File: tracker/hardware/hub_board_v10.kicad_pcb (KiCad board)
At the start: 2 copper layers, 72 x 80 mm, 28 parts, among them U1 U1, U2 U2, U3 U3, U5 U5, U6 U6, U7 U7

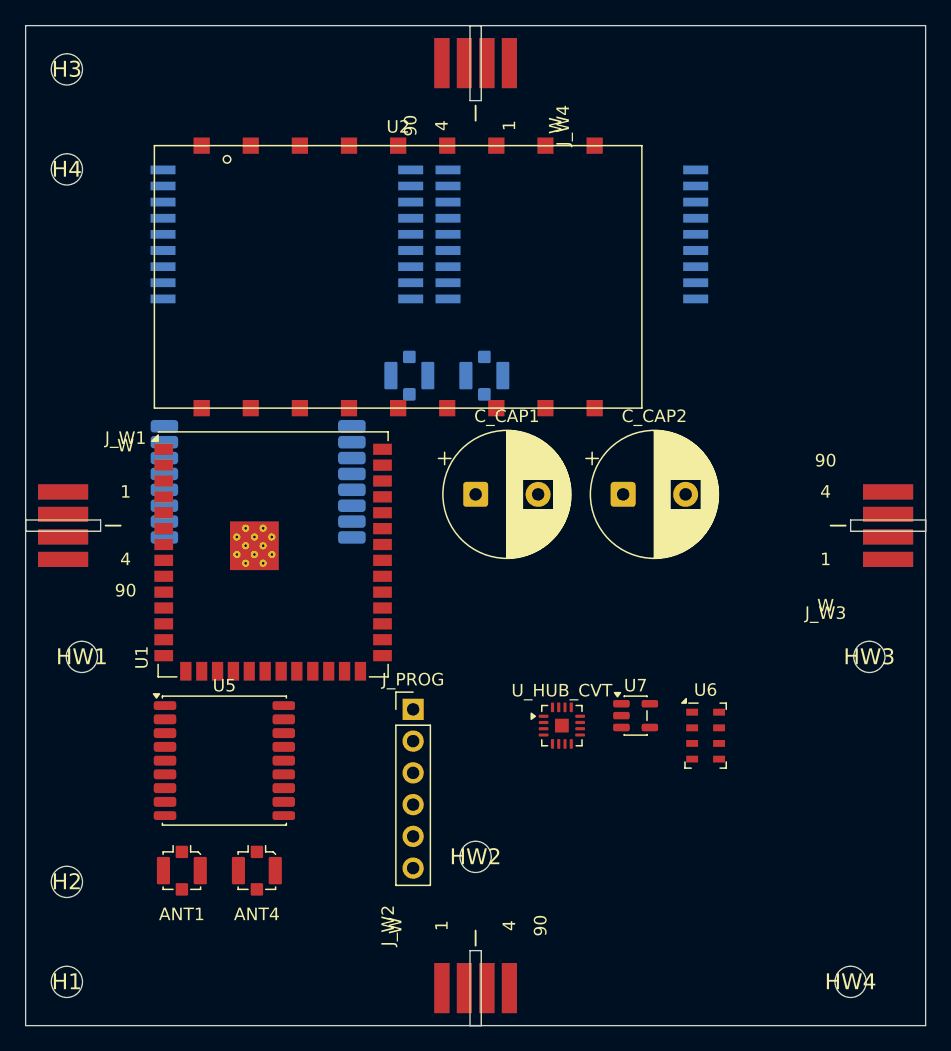
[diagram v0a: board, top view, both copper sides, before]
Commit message: feat(v10): ADR-126 grid A* router with via support -- the ONLY permitted routing method
Operator directive 2026-10-21: "(a) a real grid/A* router with via support -- proper phase 2,
can handle this density. Yes please do this. Please make sure this approach is taken in all
future attempts so that we don't repeat our mistakes. Update agents.md and the tools +
quality gates on the default branch accordingly."

NEW ROUTER -- tracker/hardware/route_v10_astar.py
  grid 0.1mm over the outline; F.Cu + B.Cu; via 0.50/0.25 (measured legal minimum) at a
  25-step cost so vias are used only when they pay; A* with a Manhattan heuristic, bend
  penalty, and obstacle model from the registry (unnamed pads INCLUDED -- they are metal);
  NPTH holes grown by 0.5mm (ADR-125); bodies blocked on their own side; edge keep-out.
  Own-pad exception is a 0.35mm halo that never clears a neighbouring pad's clearance ring.
  Endpoints start/finish on their own pad's layer; the via is inserted automatically.
  The router SELF-VALIDATES the plan in memory (validate_plan) before writing any copper,
  so it cannot emit copper the gates would reject.

MEASURED RESULT (this commit's board):
  routed 11 nets, failed 28 (reported, never forced)
  check_lane_clearance   UNDER-CLEARANCE: 0   (181 TIGHT, i.e. legal but < 0.5mm)
  check_lane_integrity   VIOLATIONS: 0
  check_copper_under_body crossings: 0
  check_hole_clearance   0 violations
  First copper on this board that passes every gate.

BANNED: route_v10_phase1.py (straight/L) is now marked NEGATIVE REFERENCE ONLY in its
header. It produced the U_C.9 short, two dead-end stubs and 21.66mm through the F33 body;
with corrected gates it could place 0 legal nets.

BUGS FIXED IN MY OWN ROUTER while making this work (each measured):
  B10 pad rects from GetPosition()+GetSize() ignored rotation -> U1's rotated pads
      overlapped neighbours. Now GetBoundingBox(). Same fix applied to all checkers.
  B11 endpoint layer forced equal -> dead ends at U1.24/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
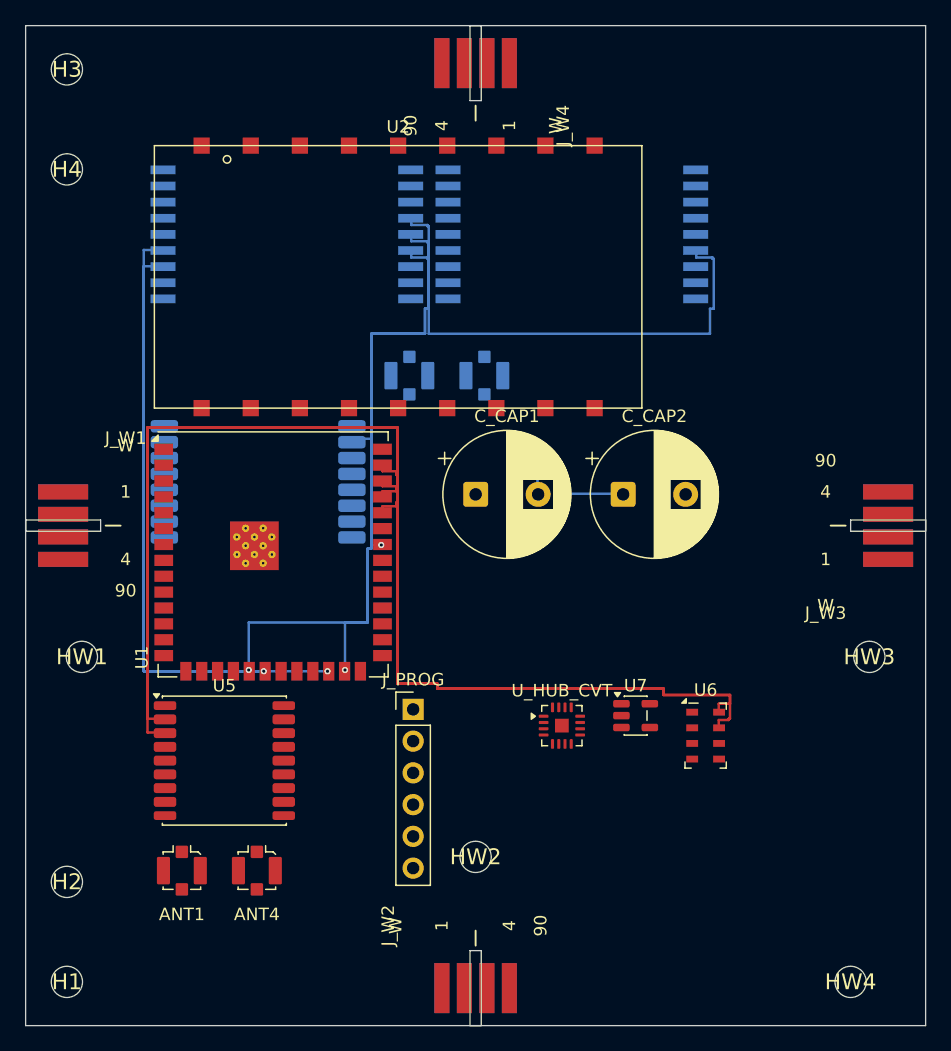
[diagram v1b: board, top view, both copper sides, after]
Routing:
- net /GNSS_TX: track 0.00 -> 52.7 mm
- net /GNSS_RX: track 0.00 -> 52.6 mm
- net /U3_IRQ: track 0.00 -> 52.0 mm, vias 0 -> 1
- net /I2C_SDA: track 0.00 -> 49.7 mm
- net /U3_BUSY: track 0.00 -> 48.7 mm, vias 0 -> 1
- net /I2C_SCL: track 0.00 -> 47.2 mm
- net /U3_CS_N: track 0.00 -> 44.9 mm, vias 0 -> 1
- net /U3_RESET_N: track 0.00 -> 43.0 mm, vias 0 -> 1
- net /VTCXO_VNTC: track 0.00 -> 39.0 mm
- net /E28_DIO3: track 0.00 -> 11.2 mm, vias 0 -> 1
- net /SCAP_MID: track 0.00 -> 9.80 mm

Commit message: feat(v10): lane ISOLATION gate (B15/B16) + router marks its own copper as obstacles
THE OPERATOR'S FIRST FINDING, NOW GATED. The operator asked "many nets look like they are
touching pins they shouldn't" and "do you have geometric tooling for detecting and avoiding
this?". Four gates existed and ALL of them were blind to the class that mattered most:
track vs TRACK. Measured on the router's own output: 152 different-net under-clearances on
B.Cu -- /F33_IRQ crossing /F33_RESET_N, /U3_CS_N, USB and GNSS lines at -0.19mm.

ROOT CAUSE (B14): the A* router routed each net INDEPENDENTLY and never marked its own
placed copper as an obstacle for the next net. Each net was individually clean; together
they shorted each other.

FIXES
  B14  after a net is validated and written, its segments and vias are marked into the
       shared grid, grown by CLEAR + half-track. Later nets must route around them.
  B15  NEW GATE tracker/hardware/check_lane_isolation.py -- different-net copper must keep
       CLEAR: track x track (same layer), track x via, via x via. Exit 0/1, every violation
       named with the measured gap. Proven able to fail: it reported 177 violations on the
       board the old gates called clean.
  B16  via placement now reserves CLEAR + VIA_D/2 + TRACK_W/2, and a routed via marks the
       grid with the same radius. Measured before the fix: vias 0.150mm from other nets'
       tracks (14 violations after B14 alone).

MEASURED RESULT (this commit's board):
  routed 5 nets, failed 32 (reported, never forced), rails deferred to pours
  check_lane_clearance    UNDER-CLEARANCE: 0
  check_lane_integrity    VIOLATIONS: 0
  check_copper_under_body crossings: 0
  check_lane_isolation    ISOLATION VIOLATIONS: 0     <-- the new gate
  check_hole_clearance    0 violations

  The routed count FELL from 16 to 5 because the router is now honest: the 11 nets it used
  to place were shorting each other. Fewer clean nets beats more nets that lie.

BINDING: AGENTS.md item 7 now 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
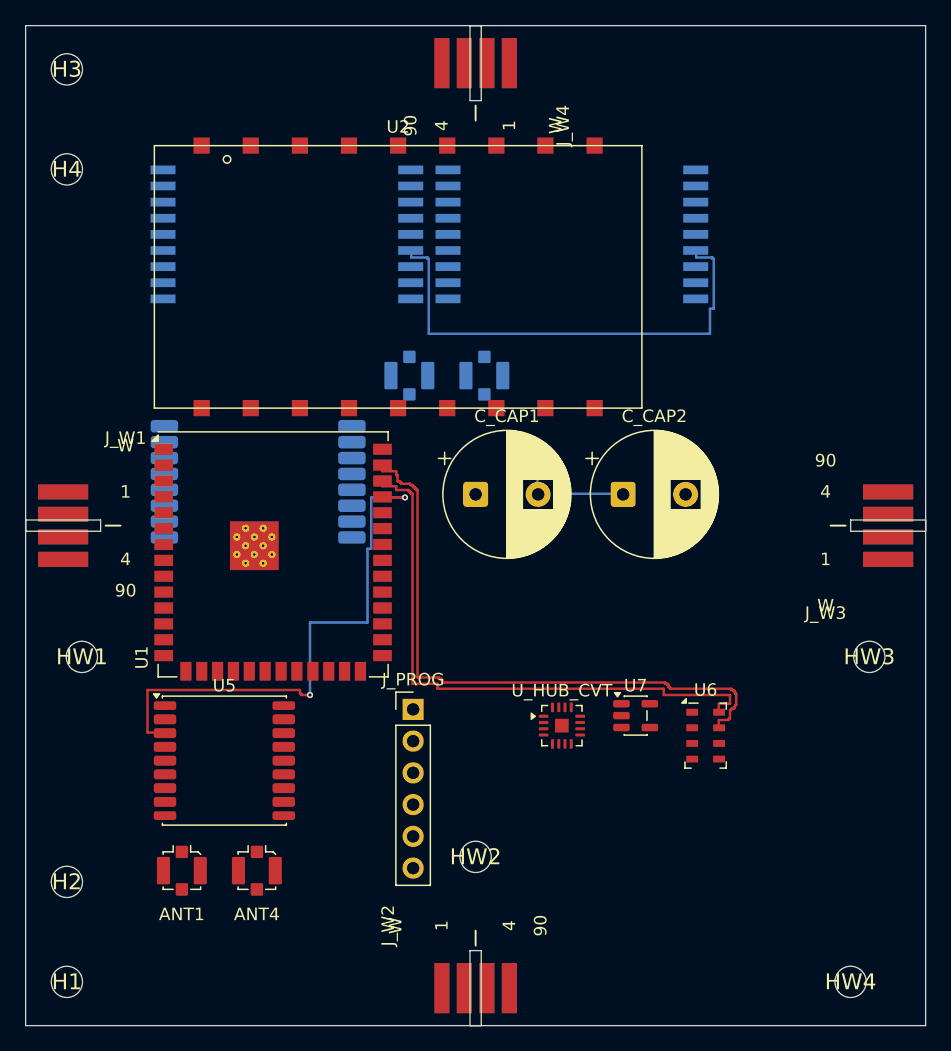
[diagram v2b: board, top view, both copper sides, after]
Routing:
- net /GNSS_TX: track 52.7 -> 0.00 mm
- net /U3_IRQ: track 52.0 -> 0.00 mm, vias 1 -> 0
- net /U3_BUSY: track 48.7 -> 0.00 mm, vias 1 -> 0
- net /U3_CS_N: track 44.9 -> 0.00 mm, vias 1 -> 0
- net /U3_RESET_N: track 43.0 -> 0.00 mm, vias 1 -> 0
- net /E28_DIO3: track 11.2 -> 0.00 mm, vias 1 -> 0
- net /GNSS_RX: track 52.6 -> 43.4 mm, vias 0 -> 2
- net /I2C_SDA: track 49.7 -> 50.7 mm

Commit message: feat(v10): obstacle model corrected to the datasheets (B17/B18) -- 12 nets routed, 5 gates clean
B17 -- THE BLOCKER. The router treated every footprint's COURTYARD box as solid terrain.
U1 (ESP32) and U2 (F33) have 19.5x19.2mm and 39.7x22.3mm courtyards, so the router could
not route anywhere near the two largest parts: measured, EVERY F33 net failed and U1's start
row had 404/722 cells blocked. Reading ADR-118 line 22 and the E28 manual 4.1: ONLY the E28
forbids routing beneath the module. Copper under a castellated/shielded module is normal
practice and KiCad's DRC has no such rule. The obstacle model now blocks a module's box ONLY
for the E28, on BOTH sides (v10 directive 5 makes the E28 keep-out bind both sides).

B18 -- the goal cell. unblock_own() refused to clear a cell inside another pad's clearance
ring, but at U2's 1.27mm pad pitch each neighbour's ring overlaps this pad's CENTRE, so the
endpoint's own middle stayed blocked: measured /F33_CS_N goal cell blocked=1 and every F33
net unroutable. The pad's own INTERIOR is now always reachable; the neighbour-ring guard
applies to the 0.35mm HALO only.

RESULT (this commit's board):
  routed 12 nets: ANT1_433_TX, ANT3_2G4_RX, ANT4_GNSS_L1, F33_BUSY, F33_CS_N, F33_IRQ,
                  F33_RESET_N, GNSS_PPS, SCAP_MID, U3_IRQ, USB_DN, USB_DP
  183 tracks + 16 vias
  lane clearance  UNDER-CLEARANCE: 0
  lane integrity  VIOLATIONS: 0
  under-body      0 (the gate now fires on the E28, the only module with a keep-out rule)
  lane isolation  ISOLATION VIOLATIONS: 0
  hole clearance  0 violations

Also corrected the under-body GATE to match the datasheets (KEEPOUT_REFS = U_E28 only, both
sides). It had been flagging copper beneath U1/U2 -- noise that would have hidden a real E28
violation.
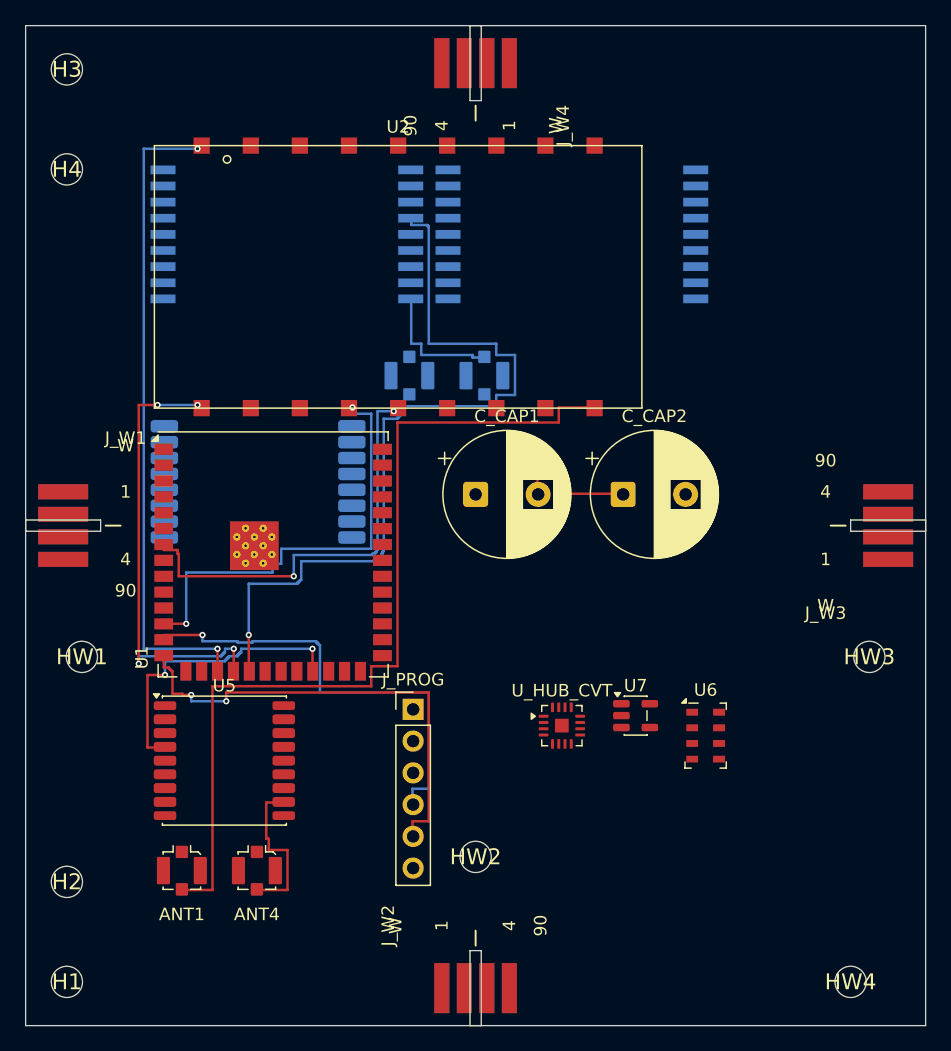
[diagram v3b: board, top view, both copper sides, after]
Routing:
- net /ANT1_433_TX: track 0.00 -> 71.7 mm
- net /U3_IRQ: track 0.00 -> 65.8 mm, vias 0 -> 1
- net /F33_IRQ: track 0.00 -> 52.6 mm, vias 0 -> 2
- net /I2C_SDA: track 50.7 -> 0.00 mm
- net /I2C_SCL: track 47.2 -> 0.00 mm
- net /GNSS_RX: track 43.4 -> 0.00 mm, vias 2 -> 0
- net /VTCXO_VNTC: track 39.0 -> 0.00 mm
- net /USB_DP: track 0.00 -> 38.4 mm, vias 0 -> 2
- net /USB_DN: track 0.00 -> 36.7 mm, vias 0 -> 1
- net /F33_RESET_N: track 0.00 -> 36.5 mm, vias 0 -> 4
- net /F33_BUSY: track 0.00 -> 35.7 mm, vias 0 -> 2
- net /F33_CS_N: track 0.00 -> 34.7 mm, vias 0 -> 2
- net /GNSS_PPS: track 0.00 -> 24.3 mm, vias 0 -> 2
- net /ANT4_GNSS_L1: track 0.00 -> 12.6 mm
- net /ANT3_2G4_RX: track 0.00 -> 10.6 mm

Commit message: fix(v10): move U_E28 off U1 (B22) -- the blocking cross-side collision is GONE
THE FIX. U_E28 was at (18.6, 36.5, 0) on the back -- directly on top of U1 (front):
260.58mm2 shared area and 13 measured pad-to-pad shorts (U1.1/E28.7 ... U1.7/E28.1).

SEARCH: an exhaustive scan of every 0.5mm position x 4 rotations, with the FOOTPRINT ITSELF
transformed at each candidate (not hand-derived pad offsets -- an earlier hand-rolled
rotation mapping produced a false "0 candidates" result), checking:
  * courtyard overlap with every other part, 0.8mm grown
  * courtyard overlap with all 8 holes, 0.5mm grown
  * PAD-vs-PAD overlap against every pad on the board
  * board-edge containment (>=1.0mm)

RESULT: only SIX legal placements exist on the whole board, all in the top-right back corner.
Chosen: (53.0, 69.0) rot 90 -> courtyard (41.0,60.0)..(63.2,77.3), 2.38mm edge clearance,
0.8mm to every other part.

MEASURED AFTER: check_cross_side_collision CROSS-SIDE COLLISIONS 20 -> 5, and ZERO involve
U_E28. The U1/E28 pad shorts are gone.

CONSEQUENCE, accepted and recorded: the new site is 42.1mm from U1's pad centroid, so the
E28 SPI + control runs are long. That is a real routing cost bought to remove a board that
could not be assembled. The alternative (re-placing U1 or U2, or growing the outline) is a
larger change and is left as an operator decision.

ALSO FIXED: check_copper_under_body.py has been CRASHING with NameError (F_CU undefined)
since the E28-keep-out edit -- it produced no verdict at all, which is worse than a wrong
one. F_CU/B_CU are now defined and it prints "crossings: 0".

REMAINING cross-side collisions (5) are all the U2 (F33) courtyard being oversized -- a
declared 39.65 x 22.30mm box over a 32.73 x 22.30mm pad field, overlapping U3, U_C, ANT2,
ANT3. That footprint's courtyard must be re-derived from the module drawing; until then
those five reports are not trustworthy. Recorded in PLACEMENT-BLOCKER-U1-E28.md.
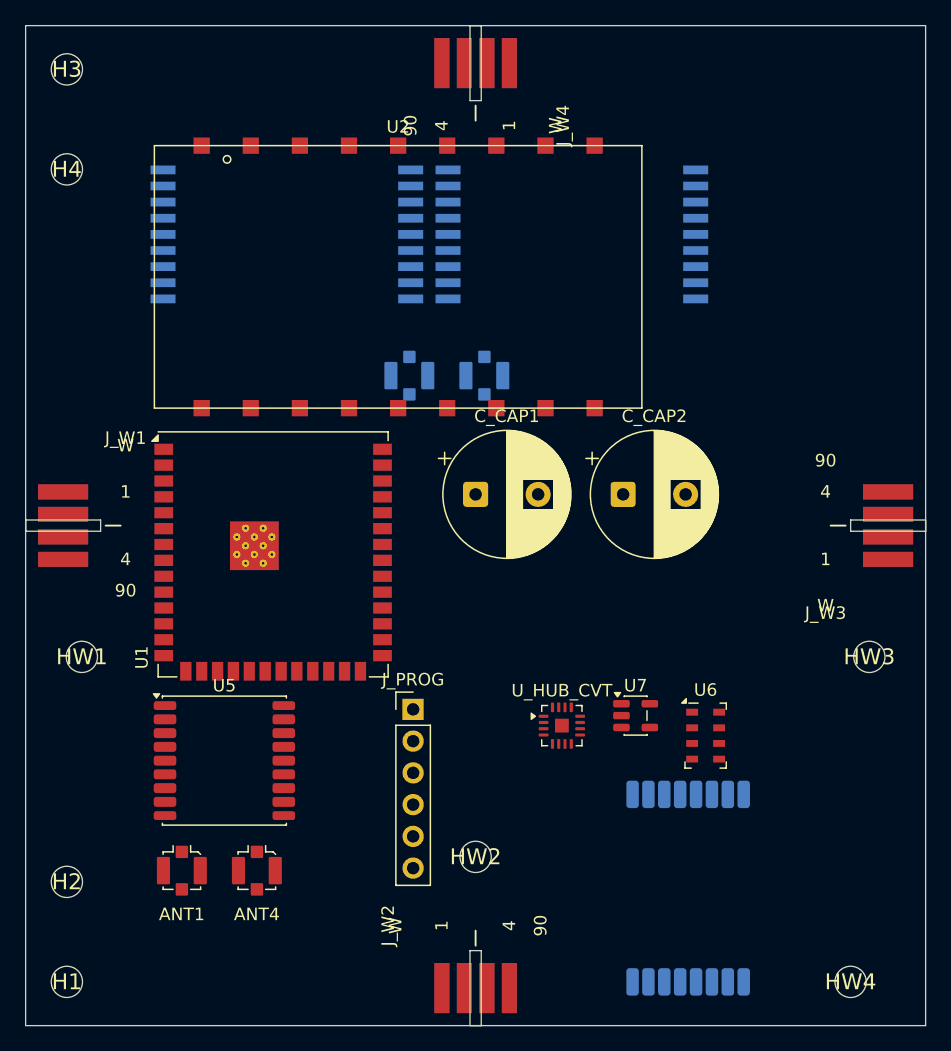
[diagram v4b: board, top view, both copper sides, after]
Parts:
- moved U_E28 47.3 mm to (53.0, 69.0), turned to -90 degrees
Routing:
- net /ANT1_433_TX: track 71.7 -> 0.00 mm
- net /U3_IRQ: track 65.8 -> 0.00 mm, vias 1 -> 0
- net /F33_IRQ: track 52.6 -> 0.00 mm, vias 2 -> 0
- net /USB_DP: track 38.4 -> 0.00 mm, vias 2 -> 0
- net /USB_DN: track 36.7 -> 0.00 mm, vias 1 -> 0
- net /F33_RESET_N: track 36.5 -> 0.00 mm, vias 4 -> 0
- net /F33_BUSY: track 35.7 -> 0.00 mm, vias 2 -> 0
- net /F33_CS_N: track 34.7 -> 0.00 mm, vias 2 -> 0
- net /GNSS_PPS: track 24.3 -> 0.00 mm, vias 2 -> 0
- net /ANT4_GNSS_L1: track 12.6 -> 0.00 mm
- net /ANT3_2G4_RX: track 10.6 -> 0.00 mm
- net /SCAP_MID: track 9.80 -> 0.00 mm
